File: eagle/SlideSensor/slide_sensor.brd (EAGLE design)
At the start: 104.1 x 22.9 mm, 13 parts

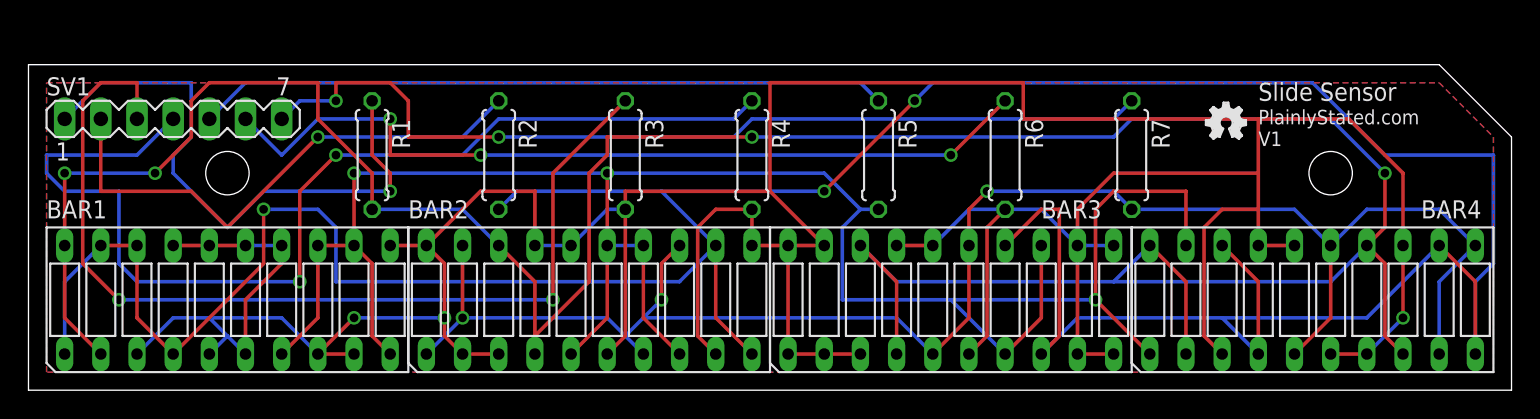
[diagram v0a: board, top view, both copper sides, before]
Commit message: v2 - fix bad schematic
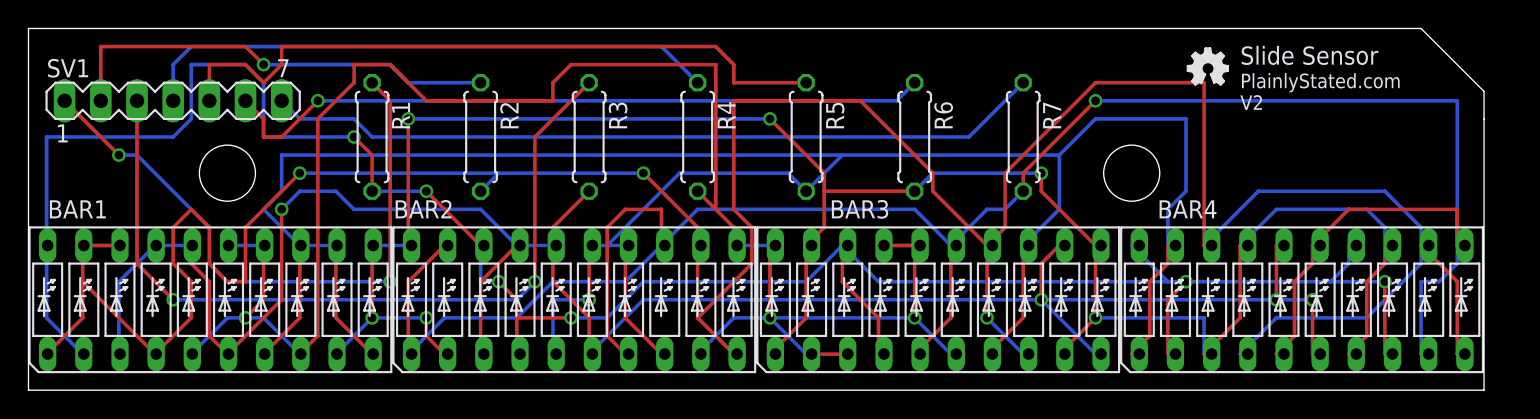
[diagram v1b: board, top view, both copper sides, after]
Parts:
- moved R7 7.73 mm to (68.6, 16.5)
- moved R6 6.48 mm to (61.0, 16.5)
- moved R5 5.24 mm to (53.3, 16.5)
- moved R4 4.02 mm to (45.7, 16.5)
- moved U$1 4.02 mm to (80.1, 20.2)
- moved R3 2.84 mm to (38.1, 16.5)
- moved R2 1.80 mm to (30.5, 16.5)
- moved R1 1.27 mm to (22.9, 16.5)
- moved SV1 1.27 mm to (8.89, 19.1)
- moved BAR1 1.19 mm to (11.5, 5.08)
- moved BAR2 1.04 mm to (37.1, 5.08)
- moved BAR3 0.89 mm to (62.6, 5.08)
- moved BAR4 0.74 mm to (88.2, 5.08)
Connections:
- net N$11 renamed N$L7
- net N$17 renamed N$P6
- net N$21 renamed N$P5
- net N$23 renamed N$L5
- net N$25 renamed N$P3
- net N$3 renamed N$P4
- net N$4 renamed N$P2
- net N$5 renamed N$L2
- net N$6 renamed N$L1
- net N$7 renamed N$P7
- net N$8 renamed N$P1
- removed net N$9: BAR1.11, BAR1.14, BAR1.15, BAR1.16, BAR1.17, BAR1.3, BAR1.5, BAR1.6, BAR1.8, BAR1.9, BAR2.11, BAR2.16, BAR2.17, BAR2.2, BAR2.20, BAR2.3, BAR2.6, BAR2.9, BAR3.1, BAR3.10, BAR3.11, BAR3.12, BAR3.16, BAR3.17, BAR3.19, BAR3.2, BAR3.20, BAR3.3, BAR3.6, BAR3.9, BAR4.13, BAR4.16, BAR4.17, BAR4.3, BAR4.6, BAR4.7, R3.2, R4.2, R6.2
- new net N$L3: BAR1.16, BAR1.17, BAR1.3, BAR1.6, BAR2.16, BAR2.17, BAR2.3, BAR2.6, BAR3.10, BAR3.12, BAR4.16, BAR4.6, R3.2
- new net N$L4: BAR1.14, BAR1.15, BAR1.5, BAR1.8, BAR2.11, BAR2.9, BAR3.16, BAR3.17, BAR3.2, BAR3.20, BAR3.3, BAR3.6, R4.2
- new net N$L6: BAR1.11, BAR1.9, BAR2.2, BAR2.20, BAR3.1, BAR3.11, BAR3.19, BAR3.9, BAR4.13, BAR4.17, BAR4.3, BAR4.7, R6.2
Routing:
- net N$9: track 297.4 -> 0.00 mm, vias 3 -> 0
- net N$L6: track 0.00 -> 150.6 mm, vias 0 -> 6
- net N$L3: track 0.00 -> 149.1 mm, vias 0 -> 4
- net N$L4: track 0.00 -> 128.9 mm, vias 0 -> 3
- net N$L1: track 211.7 -> 164.2 mm, vias 4 -> 6
- net N$L7: track 120.0 -> 166.4 mm, vias 3 -> 1
- net N$P4: track 75.9 -> 40.9 mm, vias 2 -> 0
- net N$L5: track 149.0 -> 172.7 mm, vias 3 -> 1
- net N$L2: track 241.6 -> 221.7 mm
- net N$P3: track 68.5 -> 56.5 mm
- net N$P7: track 65.6 -> 54.7 mm, vias 2 -> 0
- net N$P6: track 59.6 -> 50.4 mm, vias 3 -> 1
- net N$P2: track 37.8 -> 31.5 mm
- net N$P1: track 41.6 -> 44.1 mm, vias 1 -> 2
- removed copper zone on layer 1, net N$1
- removed copper zone on layer 16, net N$2
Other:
- board size 104.1 x 22.9 mm -> 102.2 x 25.4 mm
- board text added: "PlainlyStated.com V2"
- board text removed: "PlainlyStated.com V1"
